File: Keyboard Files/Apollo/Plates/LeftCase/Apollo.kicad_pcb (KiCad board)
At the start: 2 copper layers, 160.4 x 130.2 mm, 31 parts

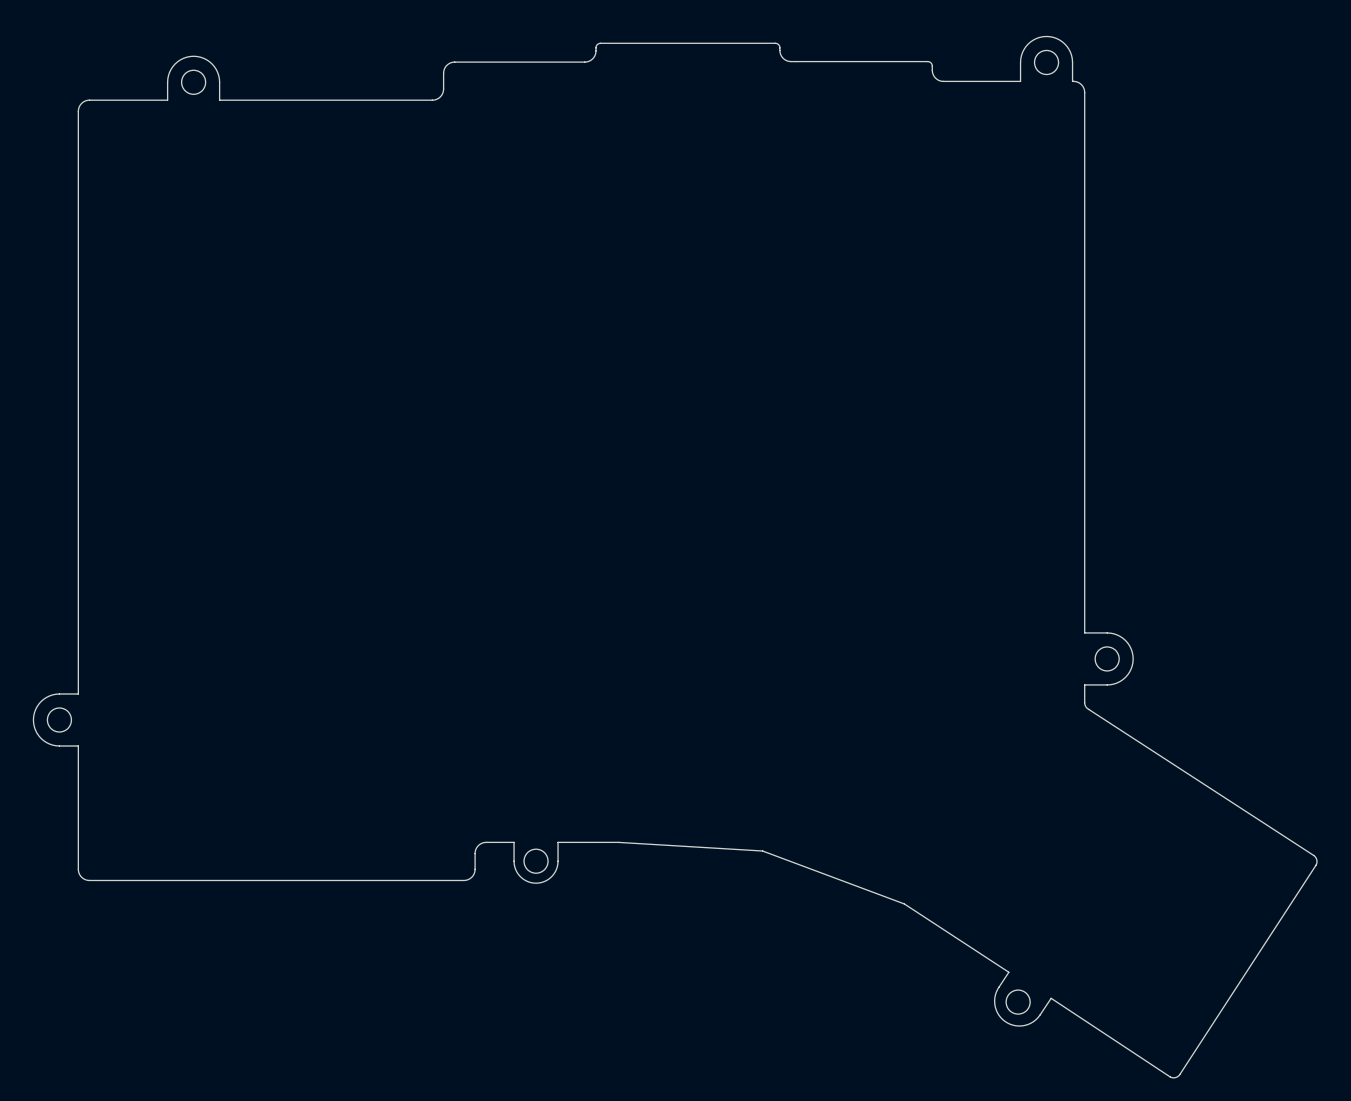
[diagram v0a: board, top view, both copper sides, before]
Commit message: Increase Apollo plate bezel
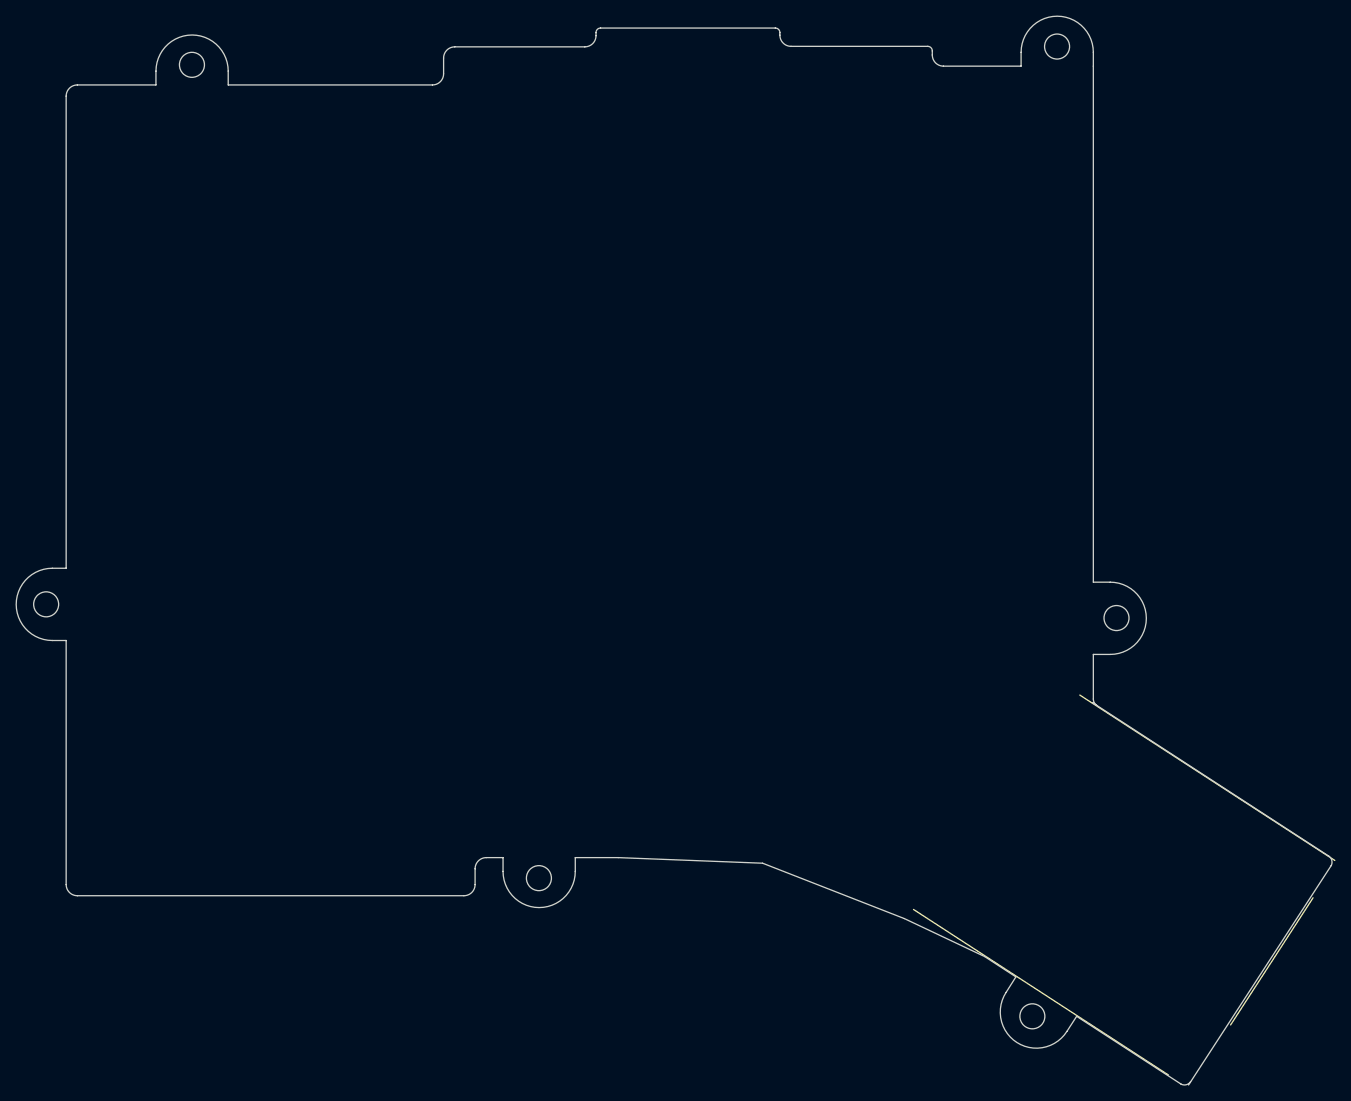
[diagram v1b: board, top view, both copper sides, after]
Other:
- board size 160.4 x 130.2 mm -> 164.5 x 133.6 mm
